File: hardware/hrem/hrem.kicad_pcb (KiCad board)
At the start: 2 copper layers, 80 x 44.4 mm, 31 parts, among them J1 AVR-ISP, J2 Hall_Conn, Q1 MMBT4401-7-F, SW1 SW_Push_Dual, U1 HT7733A, U2 ATtiny85, U3 74LVC1G125, U4 74LVC1G125

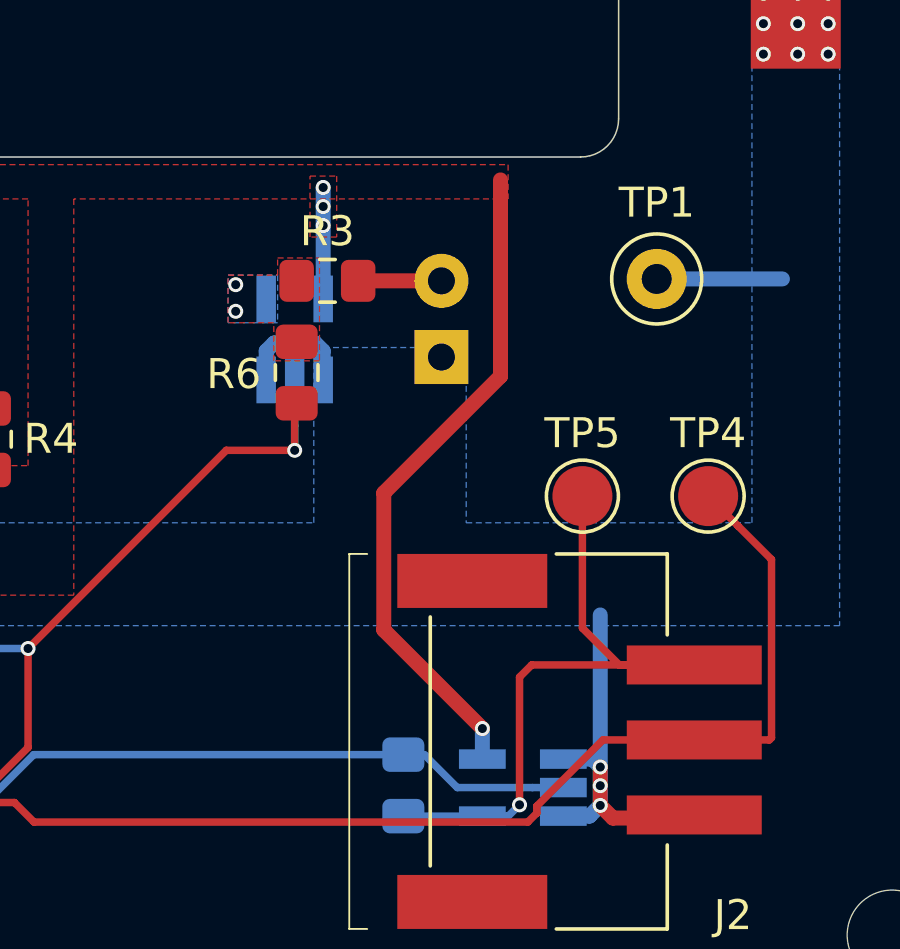
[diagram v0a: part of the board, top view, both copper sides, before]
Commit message: Decoupling caps added on U3 and U4
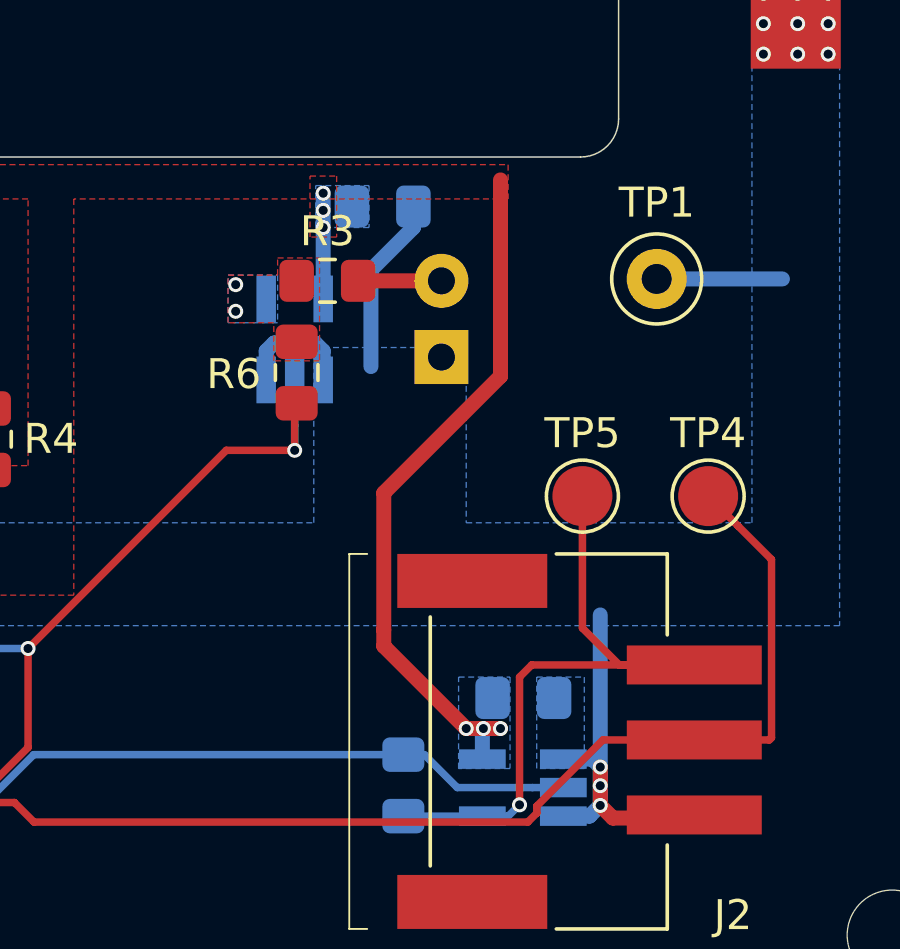
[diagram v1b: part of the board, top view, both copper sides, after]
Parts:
- added C4: 100nF, Capacitor_SMD:C_0805_2012Metric_Pad1.15x1.40mm_HandSolder, B.Cu at (115.3, 60.1)
- added C5: 100nF, Capacitor_SMD:C_0805_2012Metric_Pad1.15x1.40mm_HandSolder, B.Cu at (120.0, 76.5)
- R3: value 68R -> 100R
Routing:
- net GND: track 46.5 -> 52.4 mm
- net VCC: track 41.1 -> 41.8 mm, vias 17 -> 19
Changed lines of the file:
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@@
     (thickness 1.6)
     (drawings 14)
-    (tracks 175)
+    (tracks 183)
     (zones 0)
-    (modules 31)
+    (modules 33)
     (nets 19)
   )
@@
     (tags "SOT-23-5 hand-soldering")
     (attr smd)
-    (fp_text reference U4 (at 0 2.9) (layer B.SilkS)
+    (fp_text reference U4 (at 0 -2.7305) (layer B.SilkS)
       (effects (font (size 1 1) (thickness 0.15)) (justify mirror))
     )
@@
       (effects (font (size 1 1) (thickness 0.15)))
     )
-    (fp_text value 68R (at 0 1.65) (layer F.Fab)
+    (fp_text value 100R (at 0 1.65) (layer F.Fab)
       (effects (font (size 1 1) (thickness 0.15)))
     )
@@
     (pad "" smd rect (at 5.4 3.1 270) (size 1.8 5) (layers F.Cu F.Paste F.Mask))
     (pad "" smd rect (at -5.3 3.1 270) (size 1.8 5) (layers F.Cu F.Paste F.Mask))
+  )
+  (module Capacitor_SMD:C_0805_2012Metric_Pad1.15x1.40mm_HandSolder (layer B.Cu)
+    (at 115.325 60.071)
+    (descr "Capacitor SMD 0805 (2012 Metric), square (rectangular) end terminal, IPC_7351 nominal with elongated pad for handsoldering. (Body size source: https://docs.google.com/spreadsheets/d/1BsfQQcO9C6DZCsRaXUlFlo91Tg2WpOkGARC1WS5S8t0/edit?usp=sharing), generated with kicad-footprint-generator")
+    (tags "capacitor handsolder")
+    (attr smd)
+    (fp_text reference C4 (at 0 1.65 180) (layer B.SilkS)
+      (effects (font (size 1 1) (thickness 0.15)) (justify mirror))
+    )
+    (fp_text value 100nF (at 0 -1.65 180) (layer B.Fab)
+      (effects (font (size 1 1) (thickness 0.15)) (justify mirror))
+    )
+    (fp_line (start -1 -0.6) (end -1 0.6) (layer B.Fab) (width 0.1))
+    (fp_line (start -1 0.6) (end 1 0.6) (layer B.Fab) (width 0.1))
+    (fp_line (start 1 0.6) (end 1 -0.6) (layer B.Fab) (width 0.1))
+    (fp_line (start 1 -0.6) (end -1 -0.6) (layer B.Fab) (width 0.1))
+    (fp_line (start -0.261252 0.71) (end 0.261252 0.71) (layer B.SilkS) (width 0.12))
+    (fp_line (start -0.261252 -0.71) (end 0.261252 -0.71) (layer B.SilkS) (width 0.12))
+    (fp_line (start -1.85 -0.95) (end -1.85 0.95) (layer B.CrtYd) (width 0.05))
+    (fp_line (start -1.85 0.95) (end 1.85 0.95) (layer B.CrtYd) (width 0.05))
+    (fp_line (start 1.85 0.95) (end 1.85 -0.95) (layer B.CrtYd) (width 0.05))
+    (fp_line (start 1.85 -0.95) (end -1.85 -0.95) (layer B.CrtYd) (width 0.05))
+    (fp_text user %R (at 0 0 180) (layer B.Fab)
+      (effects (font (size 0.5 0.5) (thickness 0.08)) (justify mirror))
+    )
+    (pad 1 smd roundrect (at -1.025 0) (size 1.15 1.4) (layers B.Cu B.Paste B.Mask) (roundrect_rratio 0.217391)
+      (net 4 VCC))
+    (pad 2 smd roundrect (at 1.025 0) (size 1.15 1.4) (layers B.Cu B.Paste B.Mask) (roundrect_rratio 0.217391)
+      (net 1 GND))
+    (model ${KISYS3DMOD}/Capacitor_SMD.3dshapes/C_0805_2012Metric.wrl
+      (at (xyz 0 0 0))
+      (scale (xyz 1 1 1))
+      (rotate (xyz 0 0 0))
+    )
+  )
+  (module Capacitor_SMD:C_0805_2012Metric_Pad1.15x1.40mm_HandSolder (layer B.Cu)
+    (at 120.015 76.454)
+    (descr "Capacitor SMD 0805 (2012 Metric), square (rectangular) end terminal, IPC_7351 nominal with elongated pad for handsoldering. (Body size source: https://docs.google.com/spreadsheets/d/1BsfQQcO9C6DZCsRaXUlFlo91Tg2WpOkGARC1WS5S8t0/edit?usp=sharing), generated with kicad-footprint-generator")
+    (tags "capacitor handsolder")
+    (attr smd)
+    (fp_text reference C5 (at 0 -1.905) (layer B.SilkS)
+      (effects (font (size 1 1) (thickness 0.15)) (justify mirror))
+    )
+    (fp_text value 100nF (at 0 -1.65) (layer B.Fab)
+      (effects (font (size 1 1) (thickness 0.15)) (justify mirror))
+    )
+    (fp_text user %R (at 0 0) (layer B.Fab)
+      (effects (font (size 0.5 0.5) (thickness 0.08)) (justify mirror))
+    )
+    (fp_line (start 1.85 -0.95) (end -1.85 -0.95) (layer B.CrtYd) (width 0.05))
+    (fp_line (start 1.85 0.95) (end 1.85 -0.95) (layer B.CrtYd) (width 0.05))
+    (fp_line (start -1.85 0.95) (end 1.85 0.95) (layer B.CrtYd) (width 0.05))
+    (fp_line (start -1.85 -0.95) (end -1.85 0.95) (layer B.CrtYd) (width 0.05))
+    (fp_line (start -0.261252 -0.71) (end 0.261252 -0.71) (layer B.SilkS) (width 0.12))
+    (fp_line (start -0.261252 0.71) (end 0.261252 0.71) (layer B.SilkS) (width 0.12))
+    (fp_line (start 1 -0.6) (end -1 -0.6) (layer B.Fab) (width 0.1))
+    (fp_line (start 1 0.6) (end 1 -0.6) (layer B.Fab) (width 0.1))
+    (fp_line (start -1 0.6) (end 1 0.6) (layer B.Fab) (width 0.1))
+    (fp_line (start -1 -0.6) (end -1 0.6) (layer B.Fab) (width 0.1))
+    (pad 2 smd roundrect (at 1.025 0) (size 1.15 1.4) (layers B.Cu B.Paste B.Mask) (roundrect_rratio 0.217391)
+      (net 1 GND))
+    (pad 1 smd roundrect (at -1.025 0) (size 1.15 1.4) (layers B.Cu B.Paste B.Mask) (roundrect_rratio 0.217391)
+      (net 4 VCC))
+    (model ${KISYS3DMOD}/Capacitor_SMD.3dshapes/C_0805_2012Metric.wrl
+      (at (xyz 0 0 0))
+      (scale (xyz 1 1 1))
+      (rotate (xyz 0 0 0))
+    )
   )
   (dimension 73 (width 0.15) (layer Dwgs.User)
@@
   (segment (start 92.59748 73.025) (end 92.59748 72.39) (width 0.5) (layer F.Cu) (net 1))
   (via (at 97.79 72.263) (size 0.5) (drill 0.3) (layers F.Cu B.Cu) (net 1))
+  (segment (start 116.35 60.771) (end 114.935 62.186) (width 0.5) (layer B.Cu) (net 1))
+  (segment (start 116.35 60.071) (end 116.35 60.771) (width 0.5) (layer B.Cu) (net 1))
+  (segment (start 114.935 62.186) (end 114.935 65.405) (width 0.5) (layer B.Cu) (net 1))
   (segment (start 102.235 66.802) (end 99.441 66.802) (width 0.5) (layer F.Cu) (net 2))
   (segment (start 97.018 61.722) (end 98.36337 61.722) (width 0.5) (layer F.Cu) (net 3))
@@
   (via (at 100.0125 77.978) (size 0.5) (drill 0.3) (layers F.Cu B.Cu) (net 4))
   (segment (start 118.6485 78.4885) (end 118.6485 77.47) (width 0.5) (layer B.Cu) (net 4))
-  (via (at 118.6485 77.47) (size 0.5) (drill 0.3) (layers F.Cu B.Cu) (net 4))
+  (via (at 118.6815 77.47) (size 0.5) (drill 0.3) (layers F.Cu B.Cu) (net 4))
   (segment (start 115.361999 69.620003) (end 119.253 65.729002) (width 0.5) (layer F.Cu) (net 4))
-  (segment (start 118.6485 77.47) (end 115.361999 74.183499) (width 0.5) (layer F.Cu) (net 4))
   (segment (start 115.361999 74.183499) (end 115.361999 69.620003) (width 0.5) (layer F.Cu) (net 4))
   (segment (start 119.253 65.729002) (end 119.253 59.182) (width 0.5) (layer F.Cu) (net 4))
-  (via (at 113.3425 59.436) (size 0.5) (drill 0.3) (layers F.Cu B.Cu) (net 4))
-  (via (at 113.3425 60.071) (size 0.5) (drill 0.3) (layers F.Cu B.Cu) (net 4))
-  (via (at 113.3425 60.706) (size 0.5) (drill 0.3) (layers F.Cu B.Cu) (net 4))
-  (segment (start 113.3425 63.1495) (end 113.3425 59.436) (width 0.5) (layer B.Cu) (net 4))
+  (via (at 113.3425 59.6265) (size 0.5) (drill 0.3) (layers F.Cu B.Cu) (net 4))
+  (via (at 113.3425 60.198) (size 0.5) (drill 0.3) (layers F.Cu B.Cu) (net 4))
+  (via (at 113.3425 60.7695) (size 0.5) (drill 0.3) (layers F.Cu B.Cu) (net 4))
   (segment (start 69.85 74.422) (end 69.85 68.58) (width 0.5) (layer F.Cu) (net 4))
   (segment (start 69.85 68.58) (end 69.85 59.309) (width 0.5) (layer F.Cu) (net 4))
+  (via (at 118.11 77.47) (size 0.5) (drill 0.3) (layers F.Cu B.Cu) (net 4))
+  (via (at 119.253 77.47) (size 0.5) (drill 0.3) (layers F.Cu B.Cu) (net 4))
+  (segment (start 118.899447 77.47) (end 119.253 77.47) (width 0.5) (layer F.Cu) (net 4))
+  (segment (start 118.11 77.47) (end 118.899447 77.47) (width 0.5) (layer F.Cu) (net 4))
+  (segment (start 115.361999 74.183499) (end 115.361999 74.721999) (width 0.5) (layer F.Cu) (net 4))
+  (segment (start 115.361999 74.721999) (end 118.11 77.47) (width 0.5) (layer F.Cu) (net 4))
+  (segment (start 113.3425 63.1495) (end 113.3425 59.6265) (width 0.5) (layer B.Cu) (net 4))
   (via (at 65.151 60.579) (size 0.5) (drill 0.3) (layers F.Cu B.Cu) (net 5))
   (via (at 65.151 61.214) (size 0.5) (drill 0.3) (layers F.Cu B.Cu) (net 5))
@@
       )
     )
+  )
+  (zone (net 4) (net_name VCC) (layer B.Cu) (hatch edge 0.508)
+    (connect_pads yes (clearance 0.2))
+    (min_thickness 0.254)
+    (fill yes (arc_segments 32) (thermal_gap 0.508) (thermal_bridge_width 0.508))
+    (polygon
+      (pts
+        (xy 114.8715 60.7695) (xy 113.0935 60.7695) (xy 113.0935 59.3725) (xy 114.8715 59.3725)
+      )
+    )
+  )
+  (zone (net 4) (net_name VCC) (layer B.Cu) (hatch edge 0.508)
+    (connect_pads yes (clearance 0.2))
+    (min_thickness 0.254)
+    (fill yes (arc_segments 32) (thermal_gap 0.508) (thermal_bridge_width 0.508))
+    (polygon
+      (pts
+        (xy 119.5705 78.8035) (xy 117.856 78.8035) (xy 117.856 75.7555) (xy 119.5705 75.7555)
+      )
+    )
+  )
+  (zone (net 1) (net_name GND) (layer B.Cu) (hatch edge 0.508)
+    (connect_pads yes (clearance 0.2))
+    (min_thickness 0.254)
+    (fill yes (arc_segments 32) (thermal_gap 0.508) (thermal_bridge_width 0.508))
+    (polygon
+      (pts
+        (xy 122.047 78.8035) (xy 120.4595 78.8035) (xy 120.4595 75.7555) (xy 122.047 75.7555)
+      )
+    )

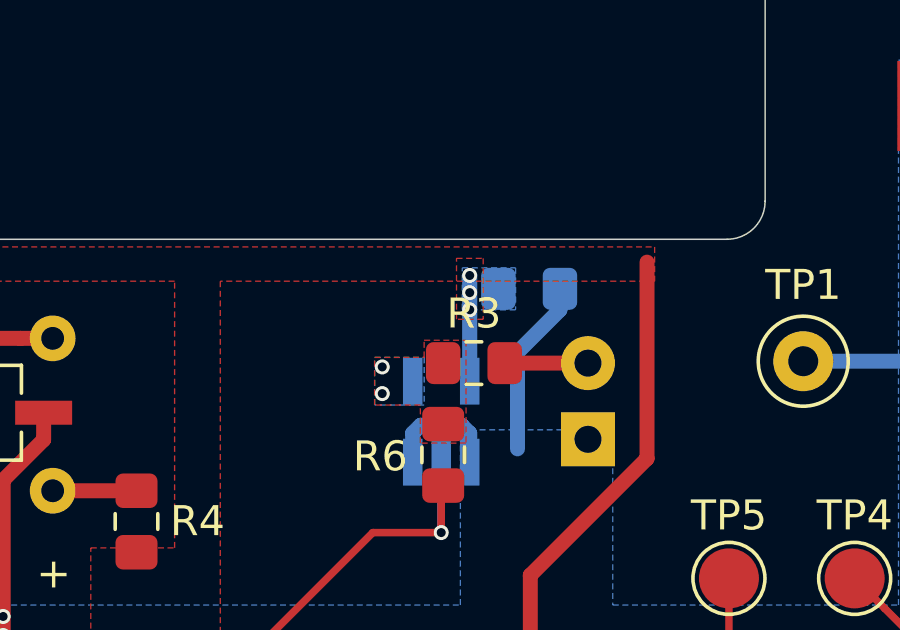
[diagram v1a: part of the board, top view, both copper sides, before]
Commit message: PCB ref names positioning and vendor part names
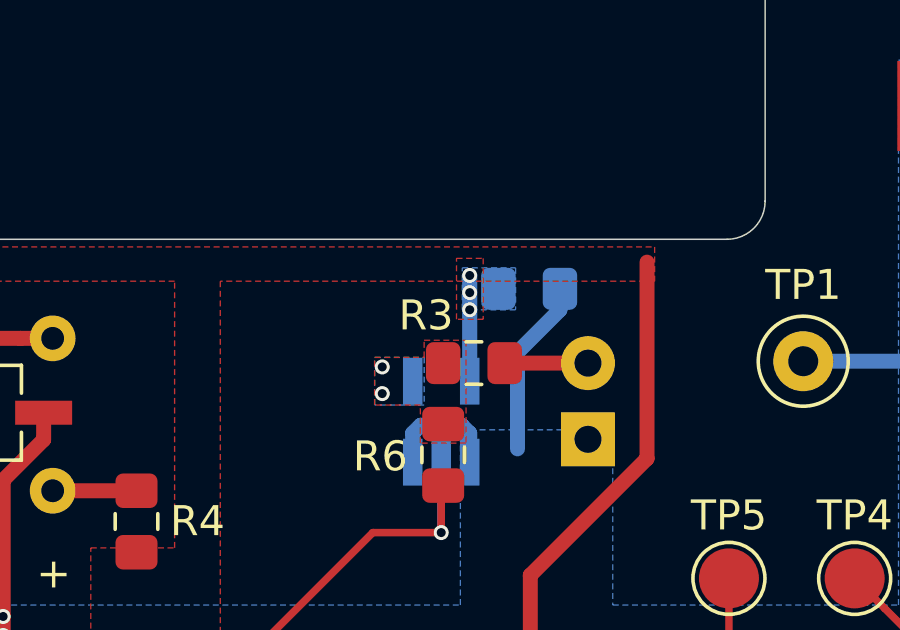
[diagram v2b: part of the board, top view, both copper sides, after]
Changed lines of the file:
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@@
   (module "hrem:Diptronics DTSM-65N" (layer B.Cu)
     (at 82.385 64.4885)
-    (fp_text reference SW1 (at -7.201 -2.2585) (layer B.SilkS)
+    (fp_text reference SW1 (at 0.038 -4.0365) (layer B.SilkS)
       (effects (font (size 1 1) (thickness 0.15)) (justify mirror))
     )
@@
     (tags "SOT-23-5 hand-soldering")
     (attr smd)
-    (fp_text reference U3 (at 3.222 0.0025 180) (layer B.SilkS)
+    (fp_text reference U3 (at -0.3975 -3.1725 180) (layer B.SilkS)
       (effects (font (size 1 1) (thickness 0.15)) (justify mirror))
     )
@@
     (tags "resistor handsolder")
     (attr smd)
-    (fp_text reference R3 (at 0 -1.65) (layer F.SilkS)
+    (fp_text reference R3 (at -1.5965 -1.5875) (layer F.SilkS)
       (effects (font (size 1 1) (thickness 0.15)))
     )
@@
     (tags "capacitor handsolder")
     (attr smd)
-    (fp_text reference C4 (at 0 1.65 180) (layer B.SilkS)
-      (effects (font (size 1 1) (thickness 0.15)) (justify mirror))
-    )
+    (fp_text reference C4 (at 3.039 0 180) (layer B.SilkS)
+      (effects (font (size 1 1) (thickness 0.15)) (justify mirror))
+    )

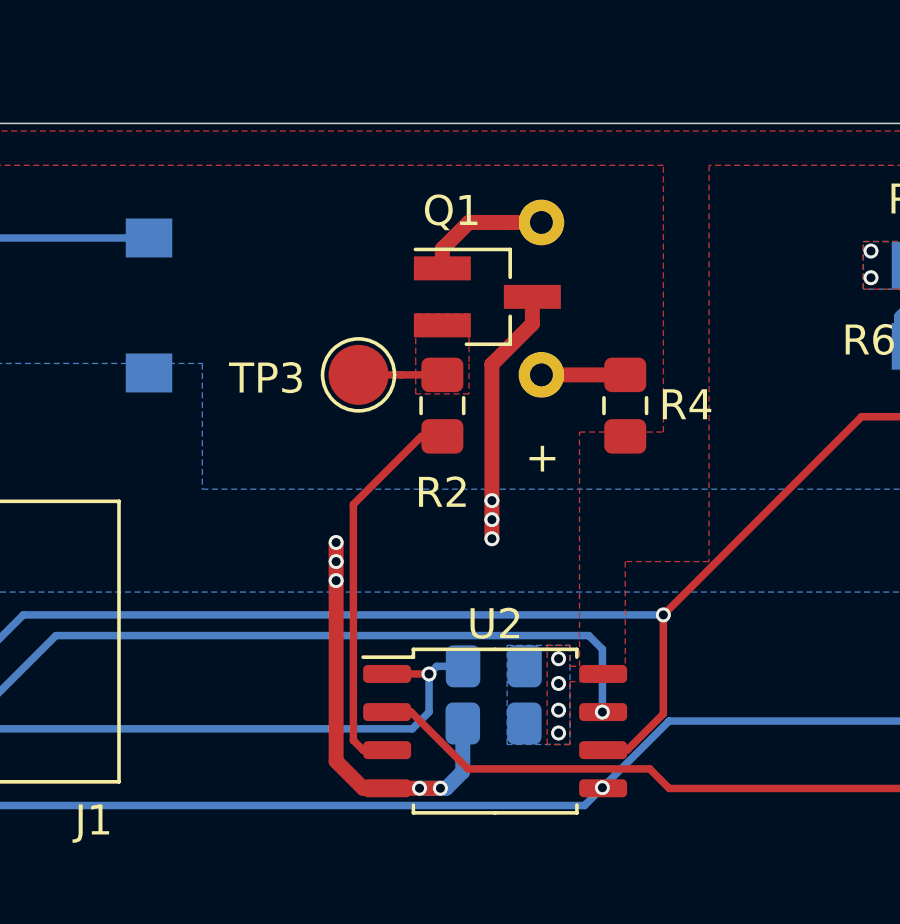
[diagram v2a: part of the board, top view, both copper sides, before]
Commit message: Fixed layout issue
Q1 has invalid schematics symbol. Base and collector was swaped.
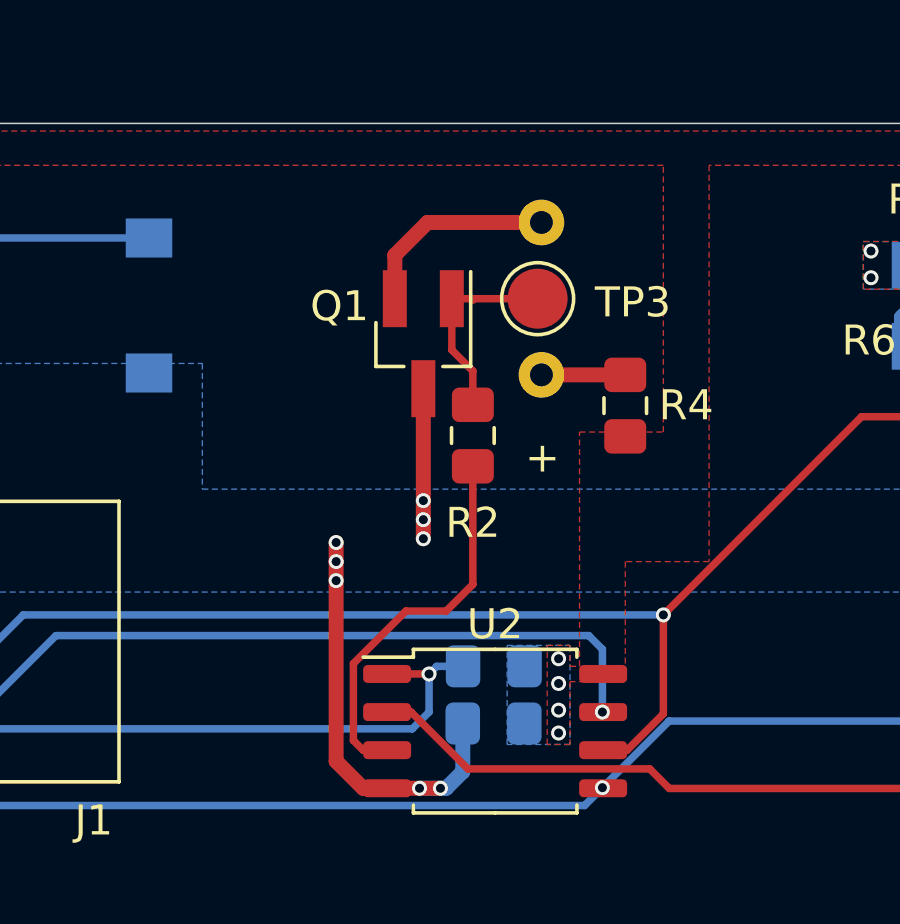
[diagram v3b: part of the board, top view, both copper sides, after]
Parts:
- moved TP3 6.49 mm to (99.3, 64.3)
- moved Q1 2.64 mm to (95.5, 65.8), turned to 270 degrees
- moved R2 1.42 mm to (97.2, 68.8)
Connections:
- Q1 pad 1: Net-(BZ1-Pad2) -> Net-(Q1-Pad1)
- Q1 pad 2: Net-(Q1-Pad2) -> Net-(BZ1-Pad2)
- R2 pad 1: Net-(Q1-Pad2) -> Net-(Q1-Pad1)
- TP3 pad 1: Net-(Q1-Pad2) -> Net-(Q1-Pad1)
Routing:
- net Net-(Q1-Pad1): track 0.00 -> 6.76 mm
- net GND: track 52.4 -> 48.8 mm
- net Net-(Q1-Pad2): track 2.79 -> 0.00 mm
- net Net-(BZ1-Pad2): track 4.32 -> 6.79 mm
- removed copper zone on F.Cu, net Net-(Q1-Pad2)
